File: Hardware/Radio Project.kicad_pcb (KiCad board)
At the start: 10 copper layers, 100 x 100 mm, 54 parts, among them J1 132225, J2 FTSH-105-X-X-DV-007-P-X, J3 132225, P1 USB_C_Plug_USB2.0, SW1 208-4, U1 Si4464, U2 Si4464, U3 STM32F407VGT6, U4 ADP2164ACPZ-3.3-R7

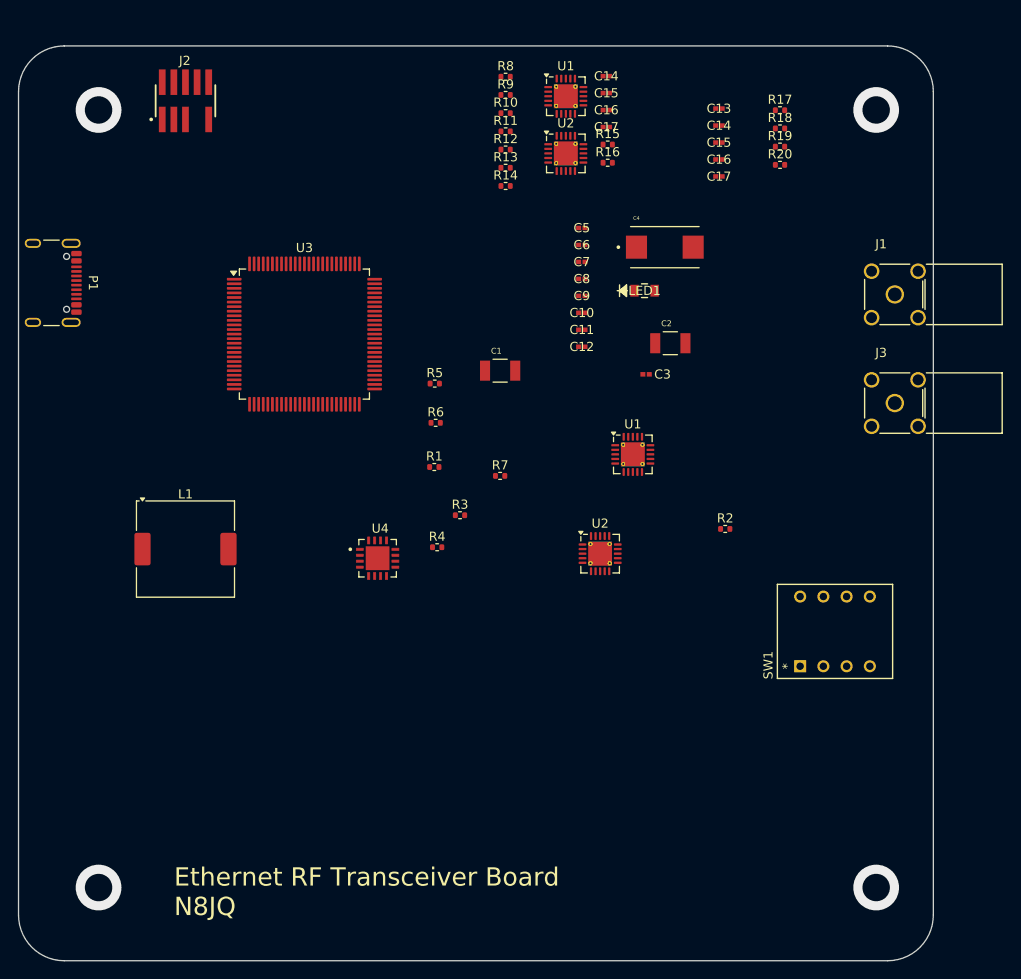
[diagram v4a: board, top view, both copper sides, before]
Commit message: shutdown pin connection to RF chain
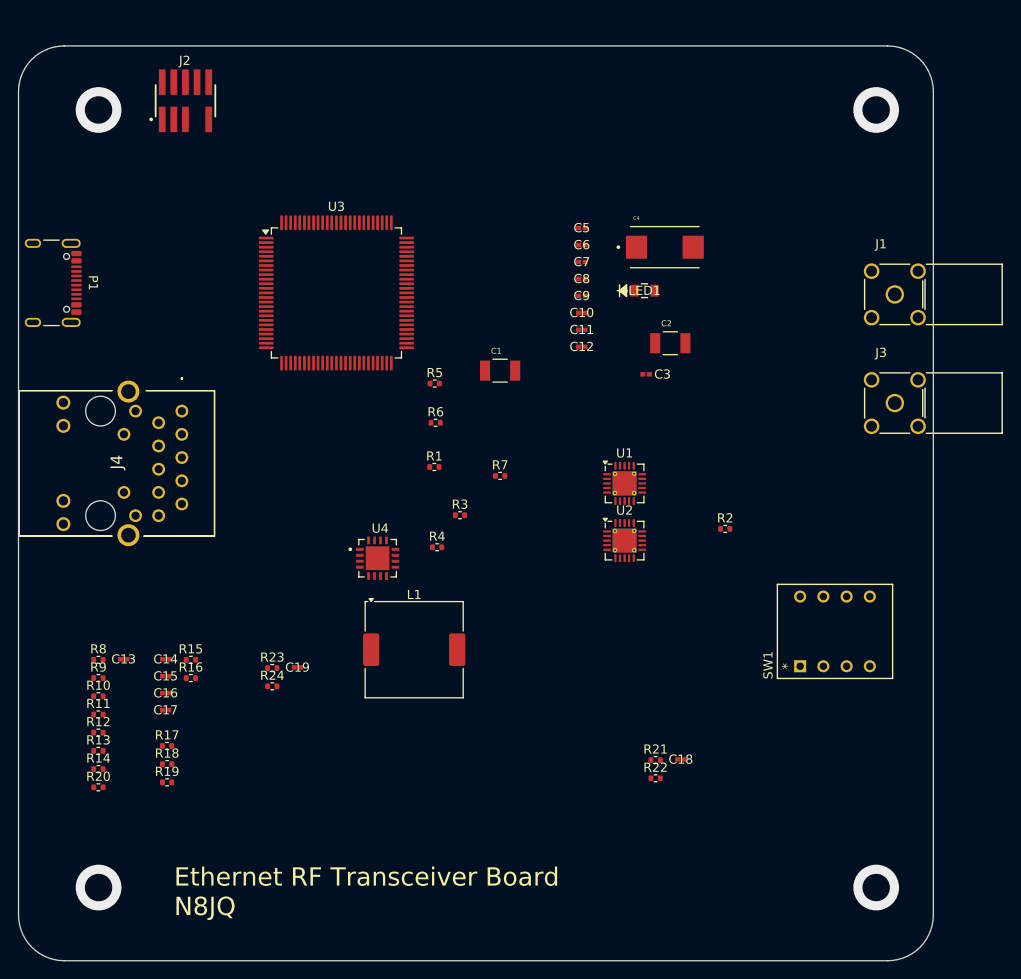
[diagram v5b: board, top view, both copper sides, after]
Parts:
- removed the C14 at (160.5, 51.3)
- removed the C14 at (172.8, 56.7)
- removed the C15 at (160.5, 53.2)
- removed the C15 at (172.8, 58.6)
- removed the C16 at (172.8, 60.4)
- removed the C16 at (160.5, 55.0)
- removed the C17 at (172.8, 62.3)
- removed the C17 at (160.5, 56.9)
- removed the U1 at (163.4, 92.7)
- removed the U1 at (156.1, 53.5)
- removed the U2 at (159.8, 103.5)
- removed the U2 at (156.1, 59.8)
- added C14: 100nF, C0402C104J8RACTU:CAPC10555_55N_KEM-L, F.Cu at (112.3, 115.0)
- added C15: 100nF, C0402C104J8RACTU:CAPC10555_55N_KEM-L, F.Cu at (112.3, 116.9)
- added C16: 100nF, C0402C104J8RACTU:CAPC10555_55N_KEM-L, F.Cu at (112.3, 118.8)
- added C17: 100nF, C0402C104J8RACTU:CAPC10555_55N_KEM-L, F.Cu at (112.3, 120.6)
- added C18: 100nF, C0402C104J8RACTU:CAPC10555_55N_KEM-L, F.Cu at (168.6, 126.0)
- added C19: 100nF, C0402C104J8RACTU:CAPC10555_55N_KEM-L, F.Cu at (126.7, 115.9)
- added J4: A70-112-331N126, A70-112-331N126:A70112331N126, F.Cu at (114.1, 87.9)
- added R21: 470, Resistor_SMD:R_0402_1005Metric, F.Cu at (165.9, 126.1)
- added R22: 470, Resistor_SMD:R_0402_1005Metric, F.Cu at (165.9, 128.1)
- added R23: 40, Resistor_SMD:R_0402_1005Metric, F.Cu at (124.0, 116.0)
- added R24: 40, Resistor_SMD:R_0402_1005Metric, F.Cu at (124.0, 118.0)
- added U1: Si4464, Package_DFN_QFN:QFN-20-1EP_4x4mm_P0.5mm_EP2.6x2.6mm_ThermalVias, F.Cu at (162.5, 95.8)
- added U2: Si4464, Package_DFN_QFN:QFN-20-1EP_4x4mm_P0.5mm_EP2.6x2.6mm_ThermalVias, F.Cu at (162.5, 102.1)
- moved R20 100.9 mm to (105.0, 129.0)
- moved R18 96.5 mm to (112.5, 126.5)
- moved R19 96.5 mm to (112.5, 128.5)
- moved R17 96.5 mm to (112.5, 124.5)
- moved C13 88.6 mm to (107.7, 115.0)
- moved R10 77.7 mm to (105.0, 119.1)
- moved R11 77.7 mm to (105.0, 121.1)
- moved R12 77.7 mm to (105.0, 123.1)
- moved R13 77.7 mm to (105.0, 125.1)
- moved R14 77.7 mm to (105.0, 127.0)
- moved R8 77.7 mm to (105.0, 115.1)
- moved R9 77.7 mm to (105.0, 117.1)
- moved R15 72.5 mm to (115.1, 115.1)
- moved R16 72.5 mm to (115.1, 117.1)
- moved L1 27.3 mm to (139.5, 114.0)
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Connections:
- U3 pad 81: unconnected-(U3-PD0-Pad81) -> Net-(U3-PD0)
- U3 pad 82: unconnected-(U3-PD1-Pad82) -> Net-(U3-PD1)
